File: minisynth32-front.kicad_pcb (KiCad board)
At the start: 2 copper layers, 15.2 x 89.9 mm, 5 parts, among them J6 R_BREAKOUT, J7 SSD1306 OLED, SW1 B1, SW3 B2

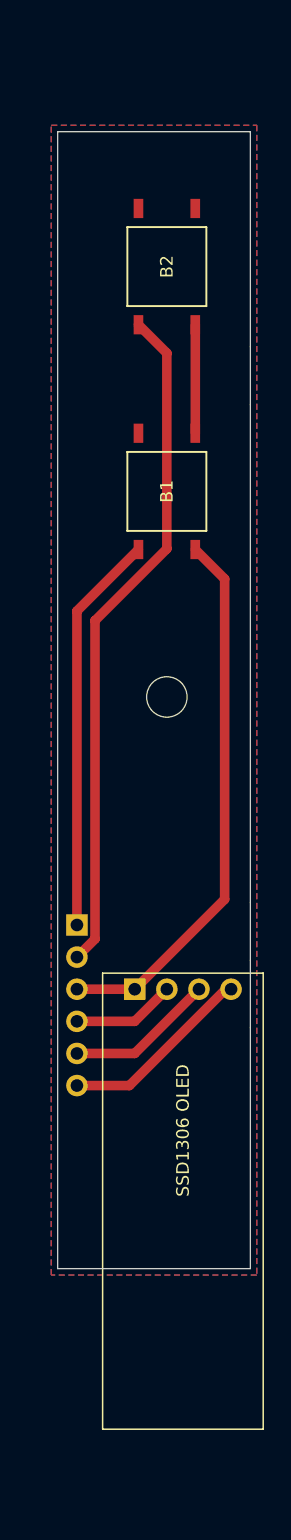
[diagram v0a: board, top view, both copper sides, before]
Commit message: Rev 1.1 F/R PCBs, tuned base and top
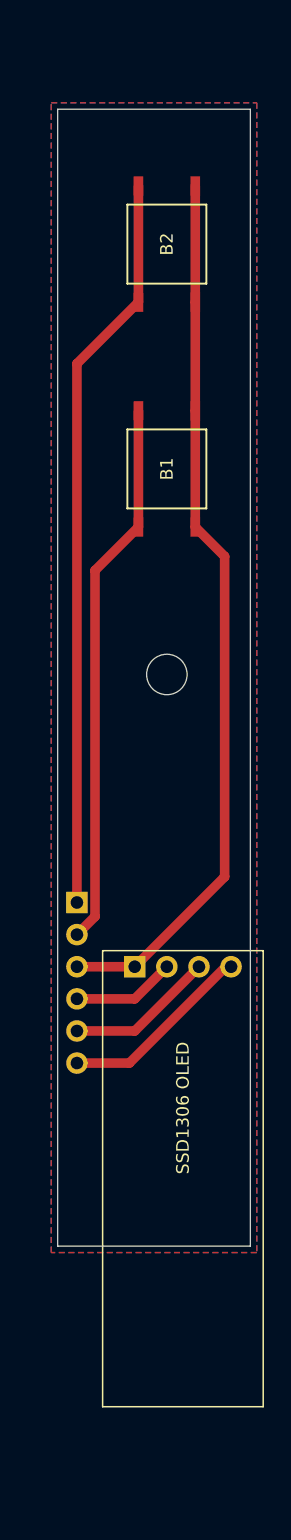
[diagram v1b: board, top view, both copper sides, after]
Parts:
- moved J6 1.78 mm to (113.3, 112.8)
- moved SW3 1.78 mm to (120.4, 60.7)
- moved J7 1.78 mm to (121.7, 134.6)
- moved REF** 1.78 mm to (120.4, 94.7)
- moved SW1 1.78 mm to (120.4, 78.5)
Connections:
- SW1 pad 2: Net-(SW1-Pad2) -> Net-(J6-Pad3)
- SW1 pad 3: Net-(J6-Pad1) -> Net-(J6-Pad2)
- SW1 pad 4: Net-(SW1-Pad4) -> Net-(J6-Pad2)
- SW3 pad 1: Net-(SW1-Pad2) -> Net-(J6-Pad3)
- SW3 pad 2: Net-(SW3-Pad2) -> Net-(J6-Pad3)
- SW3 pad 3: Net-(J6-Pad2) -> Net-(J6-Pad1)
- SW3 pad 4: Net-(SW3-Pad4) -> Net-(J6-Pad1)
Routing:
- net Net-(J6-Pad3): track 43.3 -> 70.2 mm
- net Net-(J6-Pad1): track 31.7 -> 58.7 mm
- net Net-(J6-Pad2): track 53.9 -> 43.4 mm
- net Net-(SW1-Pad2): track 8.59 -> 0.00 mm
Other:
- outline, holes or cut-outs redrawn
- board text added: "Minisynth 32: Front panel board https://github.com/grantek/minisynth32 Rev 1.1"
- board text removed: "Minisynth 32: Front panel board https://github.com/grantek/minisynth32"

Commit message: front pcb v2
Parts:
- added J8: UNUSED_2, minisynth32:PinHeader_1x04_P2.54mm_Vertical, B.Cu at (123.6, 114.8)
- added J9: UNUSED_1, minisynth32:PinHeader_1x04_P2.54mm_Vertical, B.Cu at (118.5, 114.8)
- added SW10: SW_Push, minisynth32:TL59N, F.Cu at (122.0, 79.8)
- added SW2: B2, minisynth32:TL59N, F.Cu at (122.0, 67.8)
- added SW4: SW_Push, minisynth32:TL59N, F.Cu at (122.0, 53.8)
- added SW5: SW_Push, minisynth32:TL59N, F.Cu at (115.0, 95.8)
- added SW6: SW_Push, minisynth32:TL59N, F.Cu at (115.0, 87.8)
- added SW7: SW_Push, minisynth32:TL59N, F.Cu at (115.0, 79.8)
- added SW8: SW_Push, minisynth32:TL59N, F.Cu at (122.0, 95.8)
- added SW9: SW_Push, minisynth32:TL59N, F.Cu at (122.0, 87.8)
- SW1: footprint minisynth32:TL3301AF160QG-nopaste -> minisynth32:TL59N
- SW3: value B2 -> SW_Push; footprint minisynth32:TL3301AF160QG-nopaste -> minisynth32:TL59N
- moved REF** 14.7 mm to (118.5, 109.3)
- moved SW1 12.0 mm to (115.0, 67.8), turned to 0 degrees
- moved J6 8.86 mm to (111.6, 121.5)
- moved SW3 8.76 mm to (115.0, 53.8), turned to 0 degrees
- moved J7 8.68 mm to (119.8, 143.1)
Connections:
- J6 pad 3: Net-(J6-Pad3) -> GND2
- J7 pad 1: Net-(J6-Pad3) -> GND2
- SW1 pad 1: Net-(J6-Pad3) -> Net-(J6-Pad1)
- SW1 pad 2: Net-(J6-Pad3) -> GND2
- SW3 pad 1: Net-(J6-Pad3) -> Net-(J9-Pad4)
- SW3 pad 2: Net-(J6-Pad3) -> GND2
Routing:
- net Net-(J9-Pad4): track 0.00 -> 76.7 mm
- net Net-(J6-Pad3): track 70.2 -> 0.00 mm
- net Net-(J8-Pad4): track 0.00 -> 69.7 mm
- net Net-(J9-Pad3): track 0.00 -> 43.1 mm
- net Net-(J8-Pad3): track 0.00 -> 41.8 mm
- net Net-(J9-Pad2): track 0.00 -> 32.0 mm
- net Net-(J8-Pad2): track 0.00 -> 29.4 mm
- net Net-(J8-Pad1): track 0.00 -> 19.8 mm
- net Net-(J9-Pad1): track 0.00 -> 18.2 mm
- net Net-(J6-Pad2): track 43.4 -> 60.2 mm
- net Net-(J6-Pad1): track 58.7 -> 53.2 mm
- added copper zone on B.Cu, net GND2
- removed copper zone on B.Cu, net (none)
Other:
- board size 15.2 x 89.9 mm -> 17 x 96.2 mm
- board text added: "B2 B1"
- board text added: "Minisynth 32: Front panel board Rev 2.0 https://github.com/grantek/minisynth32"
- board text added: "UNUSED"
- board text added: "UNUSED: For future expansion or fake clickable buttons."
- board text removed: "B1 B2"
- board text removed: "Minisynth 32: Front panel board https://github.com/grantek/minisynth32 Rev 1.1"

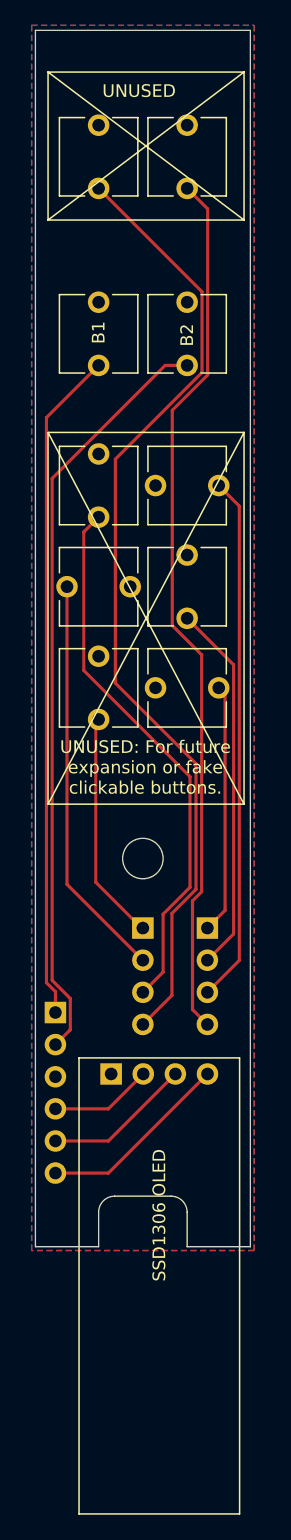
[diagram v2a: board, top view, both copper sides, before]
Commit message: Silkscreen update to front and F/R PCBs
Updated Silkscreen text for extra buttons to read "NOT FUNCTIONAL" instead of "UNUSED", and got rid of the cross through them to avoid confusion.
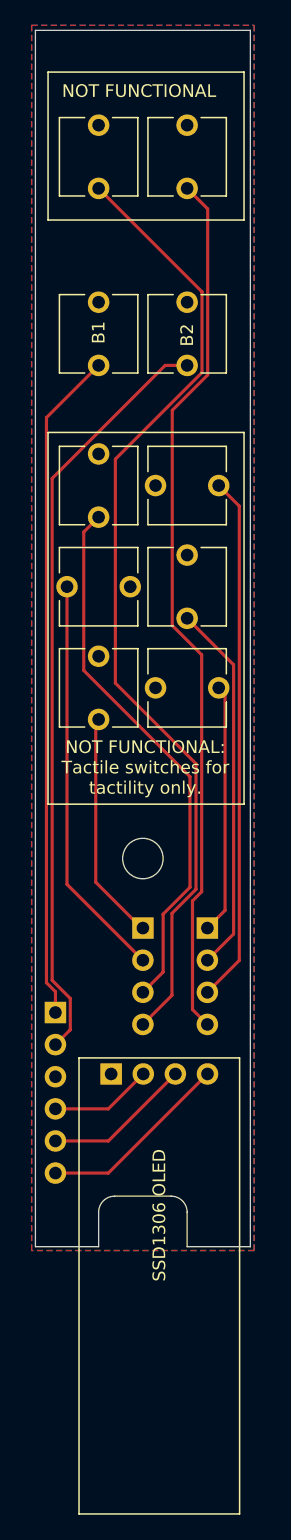
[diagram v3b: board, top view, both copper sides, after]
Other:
- board text added: "NOT FUNCTIONAL"
- board text added: "NOT FUNCTIONAL: Tactile switches for tactility only."
- board text removed: "UNUSED"
- board text removed: "UNUSED: For future expansion or fake clickable buttons."
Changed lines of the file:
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@@
   (general
     (thickness 1.6)
-    (drawings 52)
+    (drawings 48)
     (tracks 58)
     (zones 0)
@@
     (arrow2b (pts (xy 110 37.9) (xy 111.126504 37.313579)))
   )
-  (gr_text UNUSED (at 118.2 48.6) (layer F.SilkS)
+  (gr_text "NOT FUNCTIONAL" (at 118.2 48.6) (layer F.SilkS)
     (effects (font (size 1 1) (thickness 0.15)))
   )
-  (gr_line (start 126.5 58.8) (end 111 47.1) (layer F.SilkS) (width 0.12))
-  (gr_line (start 111 58.8) (end 126.5 47.1) (layer F.SilkS) (width 0.12))
   (gr_line (start 126.5 58.8) (end 111 58.8) (layer F.SilkS) (width 0.12))
   (gr_line (start 126.5 47.1) (end 126.5 58.8) (layer F.SilkS) (width 0.12))
   (gr_line (start 111 47.1) (end 126.5 47.1) (layer F.SilkS) (width 0.12))
   (gr_line (start 111 58.8) (end 111 47.1) (layer F.SilkS) (width 0.12))
-  (gr_text "UNUSED: For future\nexpansion or fake\nclickable buttons.\n\n" (at 118.7 102.9) (layer F.SilkS)
+  (gr_text "NOT FUNCTIONAL:\nTactile switches for\ntactility only." (at 118.7 102.1) (layer F.SilkS)
     (effects (font (size 1 1) (thickness 0.15)))
   )
-  (gr_line (start 111 105) (end 126.5 75.6) (layer F.SilkS) (width 0.12))
-  (gr_line (start 111 75.6) (end 126.5 105) (layer F.SilkS) (width 0.12))
   (gr_line (start 111 105) (end 111 75.6) (layer F.SilkS) (width 0.12))
   (gr_line (start 126.5 105) (end 111 105) (layer F.SilkS) (width 0.12))
